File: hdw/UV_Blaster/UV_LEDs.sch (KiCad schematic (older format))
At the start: 36 parts

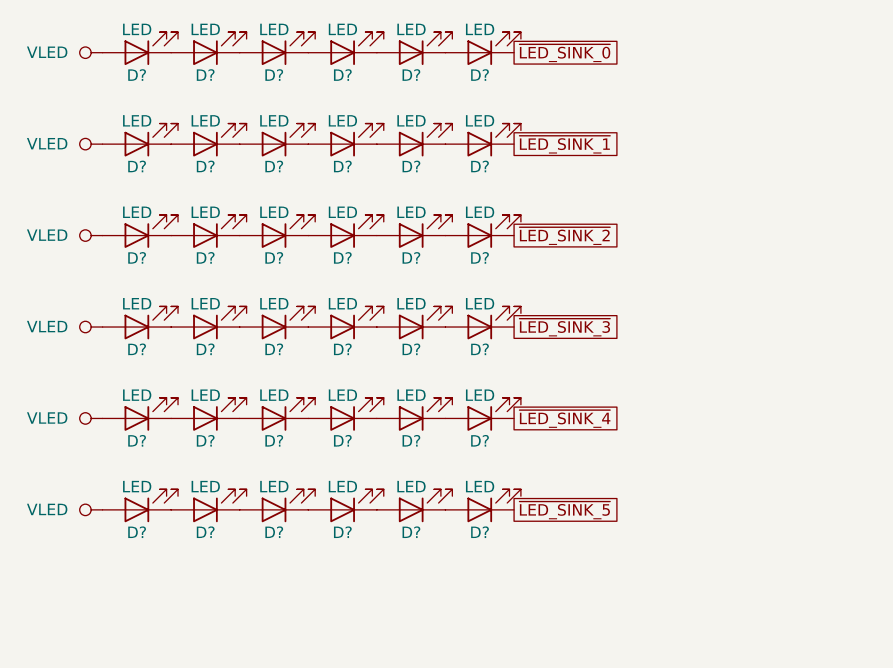
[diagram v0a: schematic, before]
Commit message: More sch work, netlist, part numbers, footprints
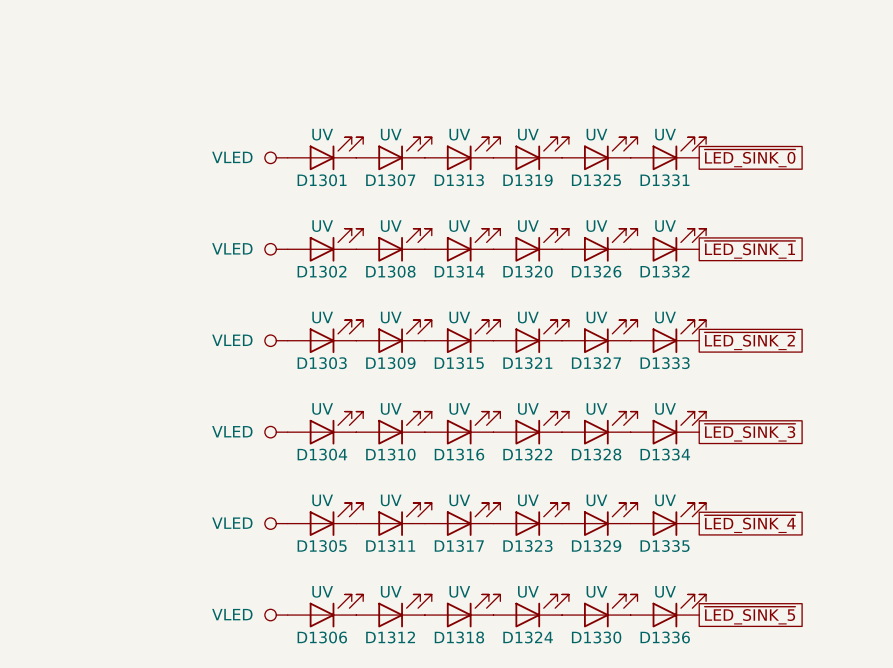
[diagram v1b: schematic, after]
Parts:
- D1301, D1302, D1303, D1304, D1305, D1306, D1307, D1308, D1309, D1310, D1311, D1312, D1313, D1314, D1315, D1316, D1317, D1318, D1319, D1320, D1321, D1322, D1323, D1324, D1325, D1326, D1327, D1328, D1329, D1330, D1331, D1332, D1333, D1334, D1335, D1336: renamed from D?; value LED -> UV; footprint (none) -> LEDs:LED_0603; Digi-Key PN (none) -> 492-1949-1-ND
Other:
- moved on the sheet: D1301, D1302, D1303, D1304, D1305, D1306, D1307, D1308, D1309, D1310, D1311, D1312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
